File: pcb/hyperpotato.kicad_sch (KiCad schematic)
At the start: 44 parts, among them J1 Conn_01x02_Socket, M1 Motor_DC, Q1 AO3401A, SW1 SW_Push_45deg, SW10 SW_Push_45deg, SW11 SW_Push_45deg, SW12 SW_Push_45deg, SW13 SW_Push_45deg, SW14 SW_SPDT, SW15 SW_Push, SW2 SW_Push_45deg, SW3 SW_Push_45deg, SW4 SW_Push_45deg, SW5 SW_Push_45deg, SW6 SW_Push_45deg, SW7 SW_Push_45deg, SW8 SW_Push_45deg, SW9 SW_Push_45deg, U1 Seeeduino Xiao nRF52840, U2 SK8707-01-SENSOR, U3 SK8707-01, U4 DRV2605LDGS

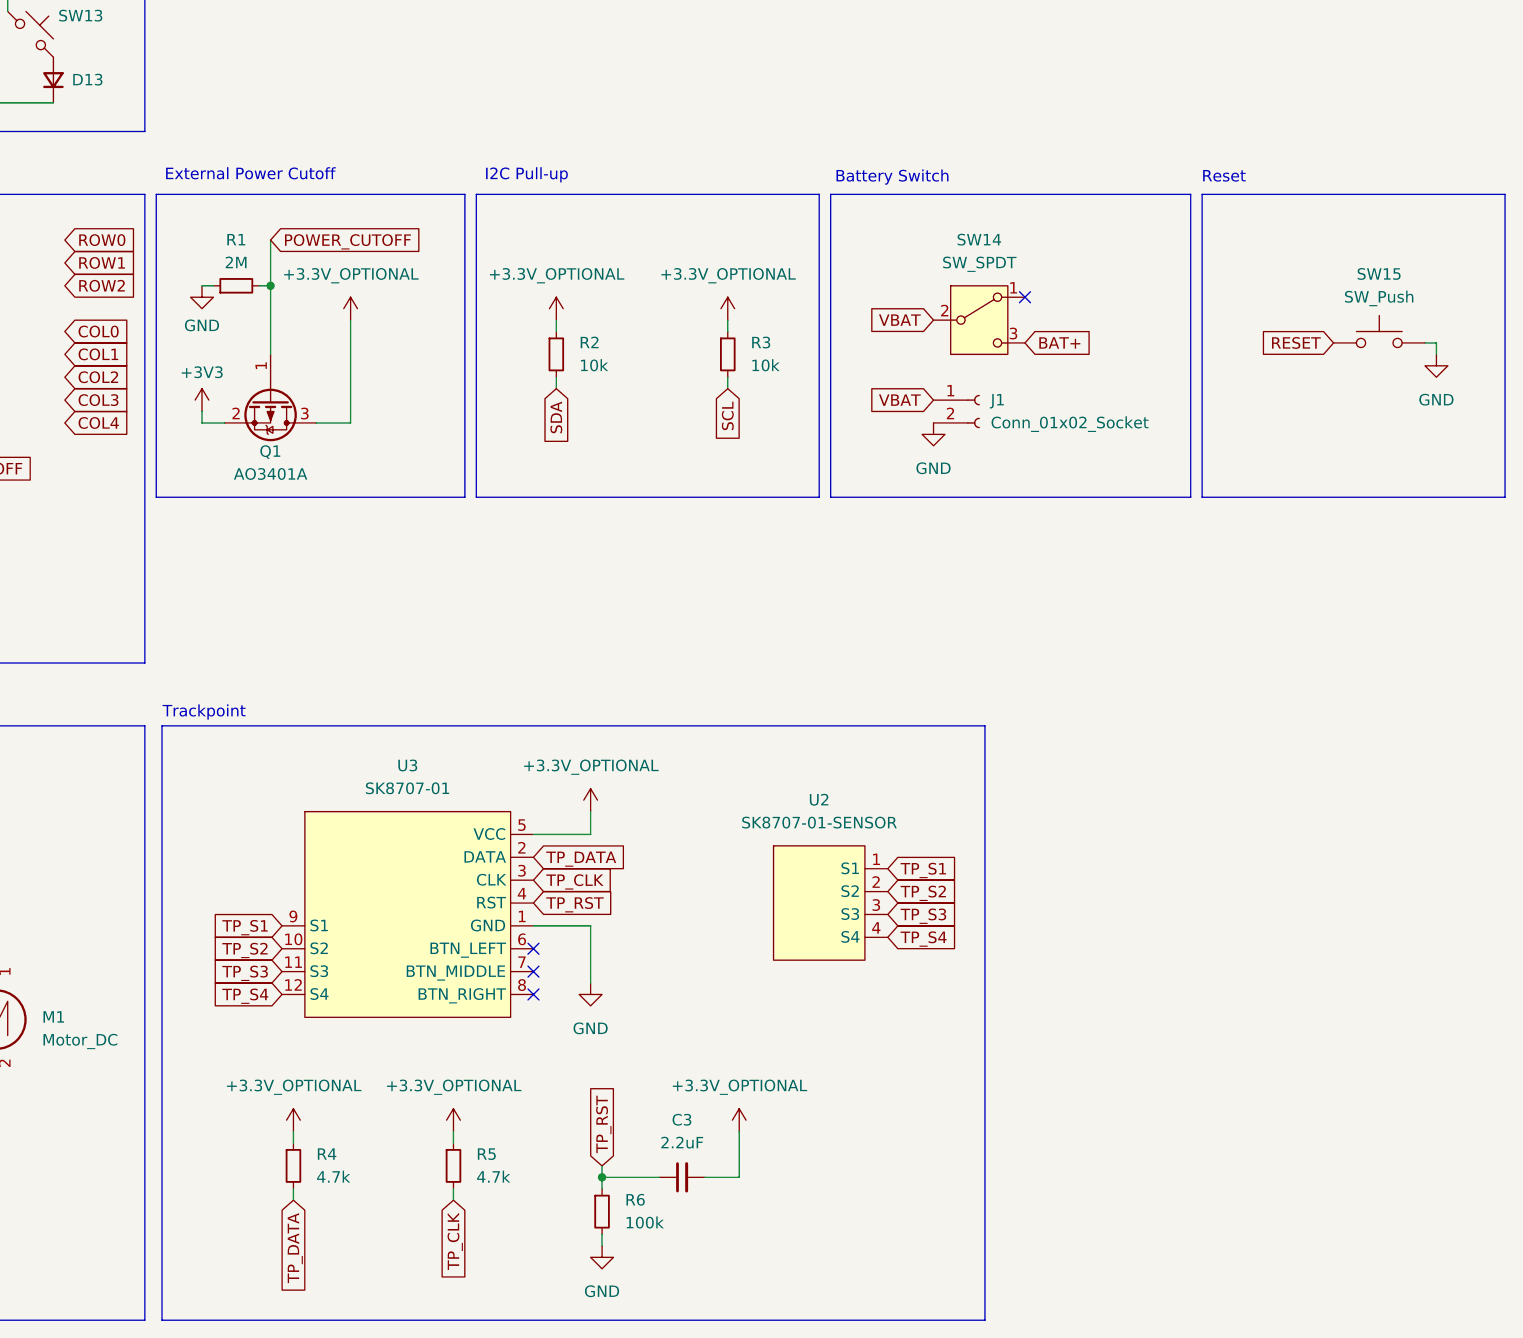
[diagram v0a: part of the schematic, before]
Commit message: Remove pullup resistors and reset circuit
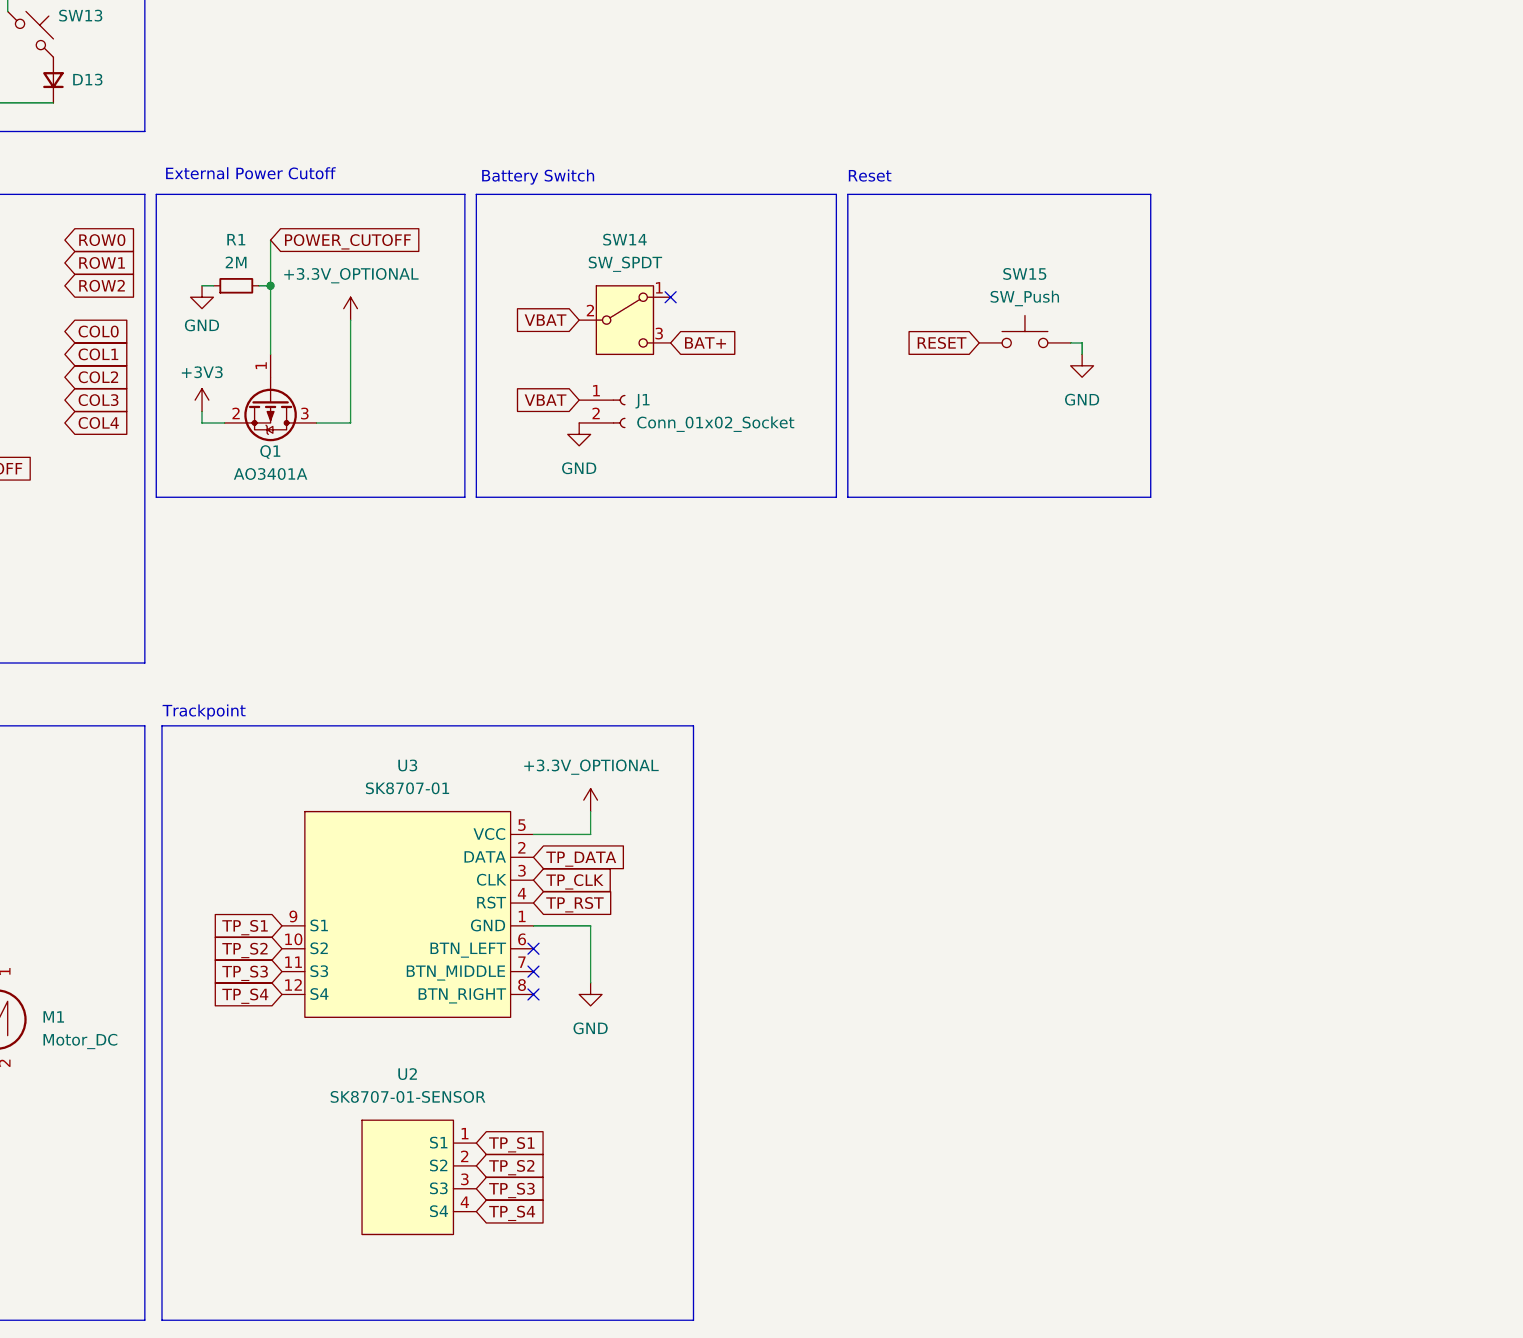
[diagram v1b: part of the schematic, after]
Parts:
- removed C3: 2.2uF, symbol Device:C_Small
- removed R2, R3: 10k, symbol Device:R_Small
- removed R4, R5: 4.7k, symbol Device:R_Small
- removed R6: 100k, symbol Device:R_Small
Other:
- note removed: "I2C Pull-up"
- moved on the sheet: J1, SW14, SW15, U2

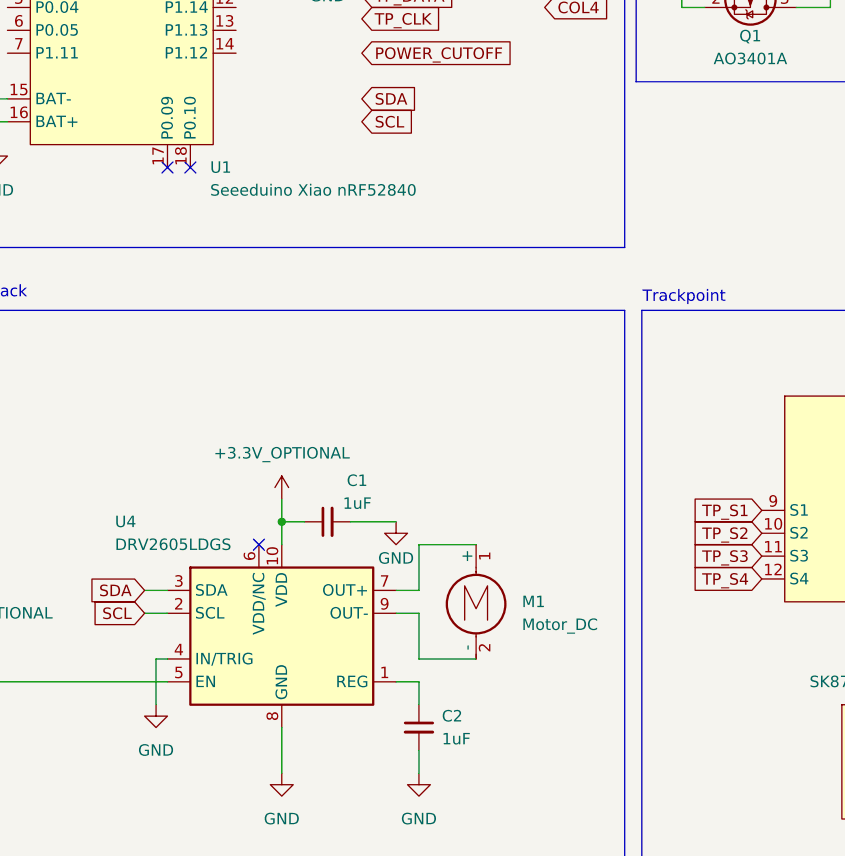
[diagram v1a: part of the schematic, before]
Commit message: Adjust main components placement
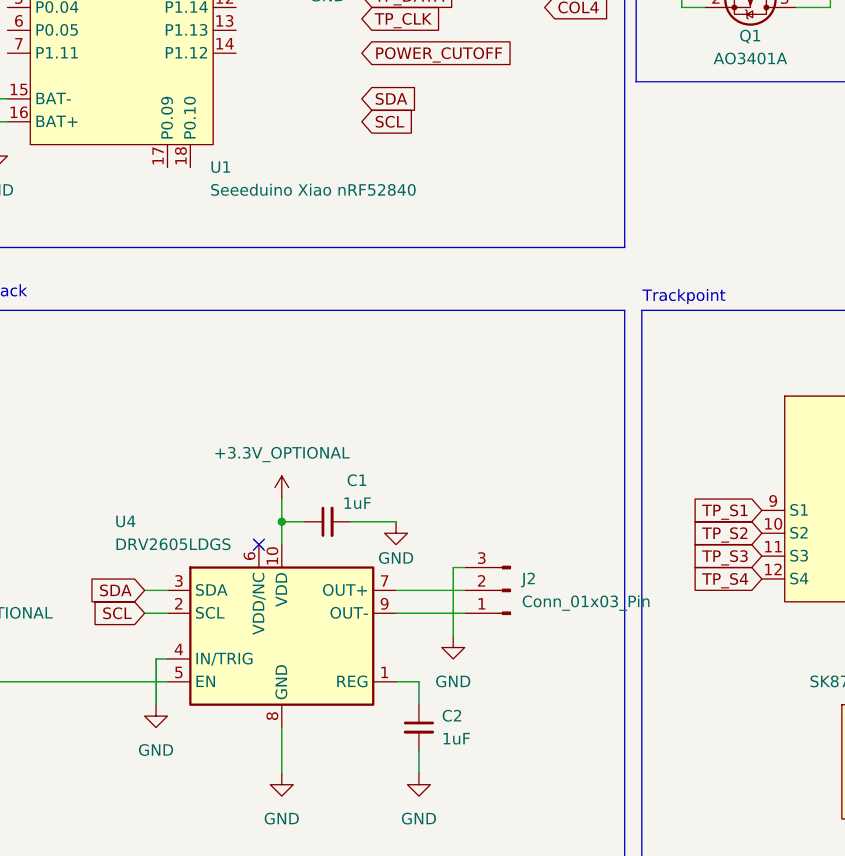
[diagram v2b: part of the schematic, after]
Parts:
- removed M1: Motor_DC, symbol Motor:Motor_DC
- added J2: Conn_01x03_Pin, ssbb_parts:ELV1411A_reversible, symbol Connector:Conn_01x03_Pin
- C1, C2: footprint (none) -> ssbb_parts:C_1206_HandSolder_reversible
- D1, D10, D11, D12, D13, D2, D3, D4, D5, D6, D7, D8, D9: footprint (none) -> ssbb_parts:D_1206_HandSolder_reversible
- J1: footprint (none) -> ssbb_parts:JST_PH_S2B-PH-K_Horizontal_reversible
- SW14: footprint (none) -> ssbb_parts:SW_SPDT_PCM12_reversible
- SW15: footprint (none) -> ssbb_parts:Panasonic_EVQPUL_EVQPUC_reversible
- U1: footprint PCM_marbastlib-xp-promicroish:Xiao_nRF52840_AC_Reflow -> ssbb_parts:Xiao_nRF52840_AC_Reflow_reversible
- U2: footprint (none) -> ssbb_parts:Sprintek_SK8707-01_Sensor; symbol hyperpotato:SK8707-01-SENSOR -> ssbb_parts:Sprintek_SK8707-01_Sensor
- U3: symbol hyperpotato:SK8707–01 -> ssbb_parts:Sprintek_SK8707–01
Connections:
- net GND: now also J2.3 (Pin_3)
- net at U4.7 (OUT+): now also J2.2 (Pin_2)
- net at U4.9 (OUT-): now also J2.1 (Pin_1)
- no-connect marks 10 -> 8
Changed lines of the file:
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@@
 	)
 	(no_connect
-		(at 48.26 124.46)
-	)
-	(no_connect
 		(at 139.7 167.64)
 	)
@@
 	)
 	(no_connect
-		(at 45.72 124.46)
-	)
-	(no_connect
 		(at 154.94 92.71)
 	)
@@
 	(wire
 		(pts
-			(xy 73.66 173.99) (xy 73.66 179.07)
-		)
-		(stroke
-			(width 0)
-			(type default)
-		)
-	)
-	(wire
-		(pts
 			(xy 60.96 71.12) (xy 73.66 71.12)
 		)
@@
 	(wire
 		(pts
-			(xy 73.66 179.07) (xy 80.01 179.07)
-		)
-		(stroke
-			(width 0)
-			(type default)
-		)
-	)
-	(wire
-		(pts
 			(xy 199.39 97.79) (xy 200.66 97.79)
 		)
@@
 	(wire
 		(pts
-			(xy 73.66 171.45) (xy 71.12 171.45)
+			(xy 71.12 171.45) (xy 78.74 171.45)
 		)
 		(stroke
@@
 	(wire
 		(pts
-			(xy 73.66 173.99) (xy 71.12 173.99)
+			(xy 71.12 173.99) (xy 78.74 173.99)
 		)
 		(stroke
@@
 	(wire
 		(pts
+			(xy 78.74 168.91) (xy 77.47 168.91)
+		)
+		(stroke
+			(width 0)
+			(type default)
+		)
+	)
+	(wire
+		(pts
 			(xy 58.42 161.29) (xy 58.42 163.83)
 		)
@@
 	(wire
 		(pts
-			(xy 80.01 166.37) (xy 73.66 166.37)
-		)
-		(stroke
-			(width 0)
-			(type default)
-		)
-	)
-	(wire
-		(pts
 			(xy 27.94 116.84) (xy 26.67 116.84)
 		)
@@
 	(wire
 		(pts
-			(xy 73.66 166.37) (xy 73.66 171.45)
-		)
-		(stroke
-			(width 0)
-			(type default)
-		)
-	)
-	(wire
-		(pts
 			(xy 102.87 106.68) (xy 105.41 106.68)
 		)
@@
 	(wire
 		(pts
+			(xy 77.47 168.91) (xy 77.47 176.53)
+		)
+		(stroke
+			(width 0)
+			(type default)
+		)
+	)
+	(wire
+		(pts
 			(xy 68.58 46.99) (xy 68.58 60.96)
 		)
@@
 			)
 		)
-		(property "Footprint" ""
+		(property "Footprint" "ssbb_parts:D_1206_HandSolder_reversible"
 			(at 73.66 54.61 90)
 			(effects
@@
 			)
 		)
-		(property "Footprint" ""
+		(property "Footprint" "ssbb_parts:D_1206_HandSolder_reversible"
 			(at 35.56 54.61 90)
 			(effects
@@
 			)
 		)
-		(property "Footprint" ""
+		(property "Footprint" "ssbb_parts:D_1206_HandSolder_reversible"
 			(at 86.36 54.61 90)
 			(effects
@@
 			)
 		)
-		(property "Footprint" ""
+		(property "Footprint" "ssbb_parts:D_1206_HandSolder_reversible"
 			(at 86.36 68.58 90)
 			(effects
@@
 			)
 		)
-		(property "Footprint" ""
+		(property "Footprint" "ssbb_parts:D_1206_HandSolder_reversible"
 			(at 48.26 41.91 90)
 			(effects
@@
 			)
 		)
-		(property "Footprint" ""
+		(property "Footprint" "ssbb_parts:Panasonic_EVQPUL_EVQPUC_reversible"
 			(at 194.31 92.71 0)
 			(effects
@@
 			)
 		)
-		(property "Footprint" ""
+		(property "Footprint" "ssbb_parts:JST_PH_S2B-PH-K_Horizontal_reversible"
 			(at 149.86 104.14 0)
 			(effects
@@
 			)
 		)
-		(property "Footprint" ""
+		(property "Footprint" "ssbb_parts:D_1206_HandSolder_reversible"
 			(at 73.66 68.58 90)
 			(effects
@@
 			)
 		)
-		(property "Footprint" "PCM_marbastlib-xp-promicroish:Xiao_nRF52840_AC_Reflow"
+		(property "Footprint" "ssbb_parts:Xiao_nRF52840_AC_Reflow_reversible"
 			(at 40.64 140.97 0)
 			(effects
@@
 			)
 		)
-		(property "Footprint" ""
+		(property "Footprint" "ssbb_parts:D_1206_HandSolder_reversible"
 			(at 48.26 68.58 90)
 			(effects
@@
 			)
 		)
-		(property "Footprint" ""
+		(property "Footprint" "ssbb_parts:D_1206_HandSolder_reversible"
 			(at 60.96 41.91 90)
 			(effects
@@
 			)
 		)
-		(property "Footprint" ""
+		(property "Footprint" "ssbb_parts:D_1206_HandSolder_reversible"
 			(at 60.96 54.61 90)
 			(effects
@@
 			)
 		)
-		(property "Footprint" ""
+		(property "Footprint" "ssbb_parts:D_1206_HandSolder_reversible"
 			(at 86.36 41.91 90)
 			(effects
@@
 			)
 		)
-		(property "Footprint" ""
+		(property "Footprint" "ssbb_parts:C_1206_HandSolder_reversible"
 			(at 63.5 163.83 0)
 			(effects
@@
 	)
 	(symbol
-		(lib_id "hyperpotato:SK8707-01-SENSOR")
+		(lib_id "ssbb_parts:Sprintek_SK8707-01_Sensor")
 		(at 125.73 190.5 0)
 		(unit 1)
@@
 			)
 		)
-		(property "Footprint" ""
+		(property "Footprint" "ssbb_parts:Sprintek_SK8707-01_Sensor"
 			(at 125.73 190.5 0)
 			(effects
@@
 			)
 		)
-		(property "Footprint" ""
+		(property "Footprint" "ssbb_parts:D_1206_HandSolder_reversible"
 			(at 73.66 41.91 90)
 			(effects
@@
 			)
 		)
-		(property "Footprint" ""
+		(property "Footprint" "ssbb_parts:D_1206_HandSolder_reversible"
 			(at 60.96 68.58 90)
 			(effects
@@
 	)
 	(symbol
-		(lib_id "hyperpotato:SK8707–01")
+		(lib_id "Connector:Conn_01x03_Pin")
+		(at 83.82 171.45 180)
+		(unit 1)
+		(exclude_from_sim no)
+		(in_bom yes)
+		(on_board yes)
+		(dnp no)
+		(fields_autoplaced yes)
+		(property "Reference" "J2"
+			(at 85.09 170.1799 0)
+			(effects
+				(font
+					(size 1.27 1.27)
+				)
+				(justify right)
+			)
+		)
+		(property "Value" "Conn_01x03_Pin"
+			(at 85.09 172.7199 0)
+			(effects
+				(font
+					(size 1.27 1.27)
+				)
+				(justify right)
+			)
+		)
+		(property "Footprint" "ssbb_parts:ELV1411A_reversible"
+			(at 83.82 171.45 0)
+			(effects
+				(font
+					(size 1.27 1.27)
+				)
+				(hide yes)
+			)
+		)
+		(property "Datasheet" "~"
+			(at 83.82 171.45 0)
+			(effects
+				(font
+					(size 1.27 1.27)
+				)
+				(hide yes)
+			)
+		)
+		(property "Description" "Generic connector, single row, 01x03, script generated"
+			(at 83.82 171.45 0)
+			(effects
+				(font
+					(size 1.27 1.27)
+				)
+				(hide yes)
+			)
+		)
+		(pin "1"
+		)
+		(pin "3"
+		)
+		(pin "2"
+		)
+		(instances
+			(project ""
+				(path "/19b5f7b9-14b9-4ffe-8621-f024a09d5ec4"
+					(reference "J2")
+					(unit 1)
+				)
+			)
+		)
+	)
+	(symbol
+		(lib_id "ssbb_parts:Sprintek_SK8707–01")
 		(at 125.73 161.29 0)
 		(unit 1)
@@
 	)
 	(symbol
-		(lib_id "Motor:Motor_DC")
-		(at 80.01 171.45 0)
+		(lib_id "power:GND")
+		(at 77.47 176.53 0)
 		(unit 1)
 		(exclude_from_sim no)
@@
 		(on_board yes)
 		(dnp no)
-		(property "Reference" "M1"
-			(at 85.09 172.7199 0)
+		(fields_autoplaced yes)
+		(property "Reference" "#PWR05"
+			(at 77.47 182.88 0)
 			(effects
 				(font
 					(size 1.27 1.27)
 				)
-				(justify left)
+				(hide yes)
 			)
 		)
-		(property "Value" "Motor_DC"
-			(at 85.09 175.2599 0)
+		(property "Value" "GND"
+			(at 77.47 181.61 0)
 			(effects
 				(font
 					(size 1.27 1.27)
 				)
-				(justify left)
 			)
 		)
 		(property "Footprint" ""
-			(at 80.01 173.736 0)
+			(at 77.47 176.53 0)
 			(effects
 				(font
@@
 			)
 		)
-		(property "Datasheet" "~"
-			(at 80.01 173.736 0)
+		(property "Datasheet" ""
+			(at 77.47 176.53 0)
 			(effects
 				(font
@@
 			)
 		)
-		(property "Description" "DC Motor"
-			(at 80.01 171.45 0)
+		(property "Description" "Power symbol creates a global label with name \"GND\" , ground"
+			(at 77.47 176.53 0)
 			(effects
 				(font
@@
 		(pin "1"
 		)
-		(pin "2"
-		)
 		(instances
 			(project ""
 				(path "/19b5f7b9-14b9-4ffe-8621-f024a09d5ec4"
-					(reference "M1")
+					(reference "#PWR05")
 					(unit 1)
 				)
@@
 			)
 		)
-		(property "Footprint" ""
+		(property "Footprint" "ssbb_parts:D_1206_HandSolder_reversible"
 			(at 48.26 54.61 90)
 			(effects
@@
 			)
 		)
-		(property "Footprint" ""
+		(property "Footprint" "ssbb_parts:SW_SPDT_PCM12_reversible"
 			(at 149.86 95.25 0)
 			(effects
@@
 			)
 		)
-		(property "Footprint" ""
+		(property "Footprint" "ssbb_parts:C_1206_HandSolder_reversible"
 			(at 73.66 186.69 0)
 			(effects
